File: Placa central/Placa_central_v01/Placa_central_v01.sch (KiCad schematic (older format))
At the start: 79 parts, among them J1 PinoCheckBateriaVcc, J10 Conn_01x01_Arduino11, J11 Conn_01x01_Arduino12, J12 Conn_01x01_Arduino13, J13 Conn_01x01_Arduino14, J14 Conn_01x01_Arduino15, J15 Conn_01x01_Arduino16, J16 PinoChargeBateriaVcc, J17 PinoChargeBateriaGND, J18 Conn_01x01_Arduino19, J19 Conn_01x01_Arduino20, J2 Conn_01x02_ArduinoTxRx, J20 Conn_01x01_Arduino21, J21 Conn_01x01_Arduino22, J22 Conn_01x01_Arduino23, J23 Conn_01x01_Arduino24, J24 Conn_01x01_Arduino25, J25 Conn_01x01_Arduino26, J26 Conn_01x01_Sensor1, J27 Conn_01x01_Sensor2, J28 Conn_01x01_Sensor3, J29 Conn_01x01_Sensor4, J3 Conn_01x01_ArduinoReset, J30 Conn_01x01_Sensor5, J31 Conn_01x01_Sensor6, J32 Conn_01x01_Sensor7, J33 Conn_01x01_SensorEsq, J34 Conn_01x01_SensorDir, J35 Conn_01x01_5VPlacaSensores, J36 Conn_01x01_GNDPlacaSensores, J37 Conn_01x01_8.4VPonteH, J38 Conn_01x01_5VPonteH, J39 Conn_01x01_GNDPonteH, J4 Conn_01x01_Arduino5, J40 Conn_01x01_Motor1PWM, J41 Conn_01x01_Motor1Dir1, J42 Conn_01x01_Motor1Dir2, J43 Conn_01x01_Motor2Dir1, J44 Conn_01x01_Motor2Dir2, J45 Conn_01x01_Motor2PWM, J46 Conn_01x02_Motor1, J47 Conn_01x02_Motor2, J48 Conn_01x01_5VEncoderEsq, J49 Conn_01x01_OutputEncoderEsq, J5 Conn_01x01_Arduino6, J50 Conn_01x01_GNDEncoderEsq, J51 Conn_01x01_5VEncoderDir, J52 Conn_01x01_OutputEncoderDir, J53 Conn_01x01_GNDEncoderDir, J6 Conn_01x01_Arduino7, J7 Conn_01x01_Arduino8, J8 Conn_01x01_Arduino9, J9 Conn_01x01_Arduino10, Q1 BC548, Q2 BC548, SW1 SW_ON/OFF, SW2 SW_AlimentacaoPlacaSensores, SW3 SW_comando1

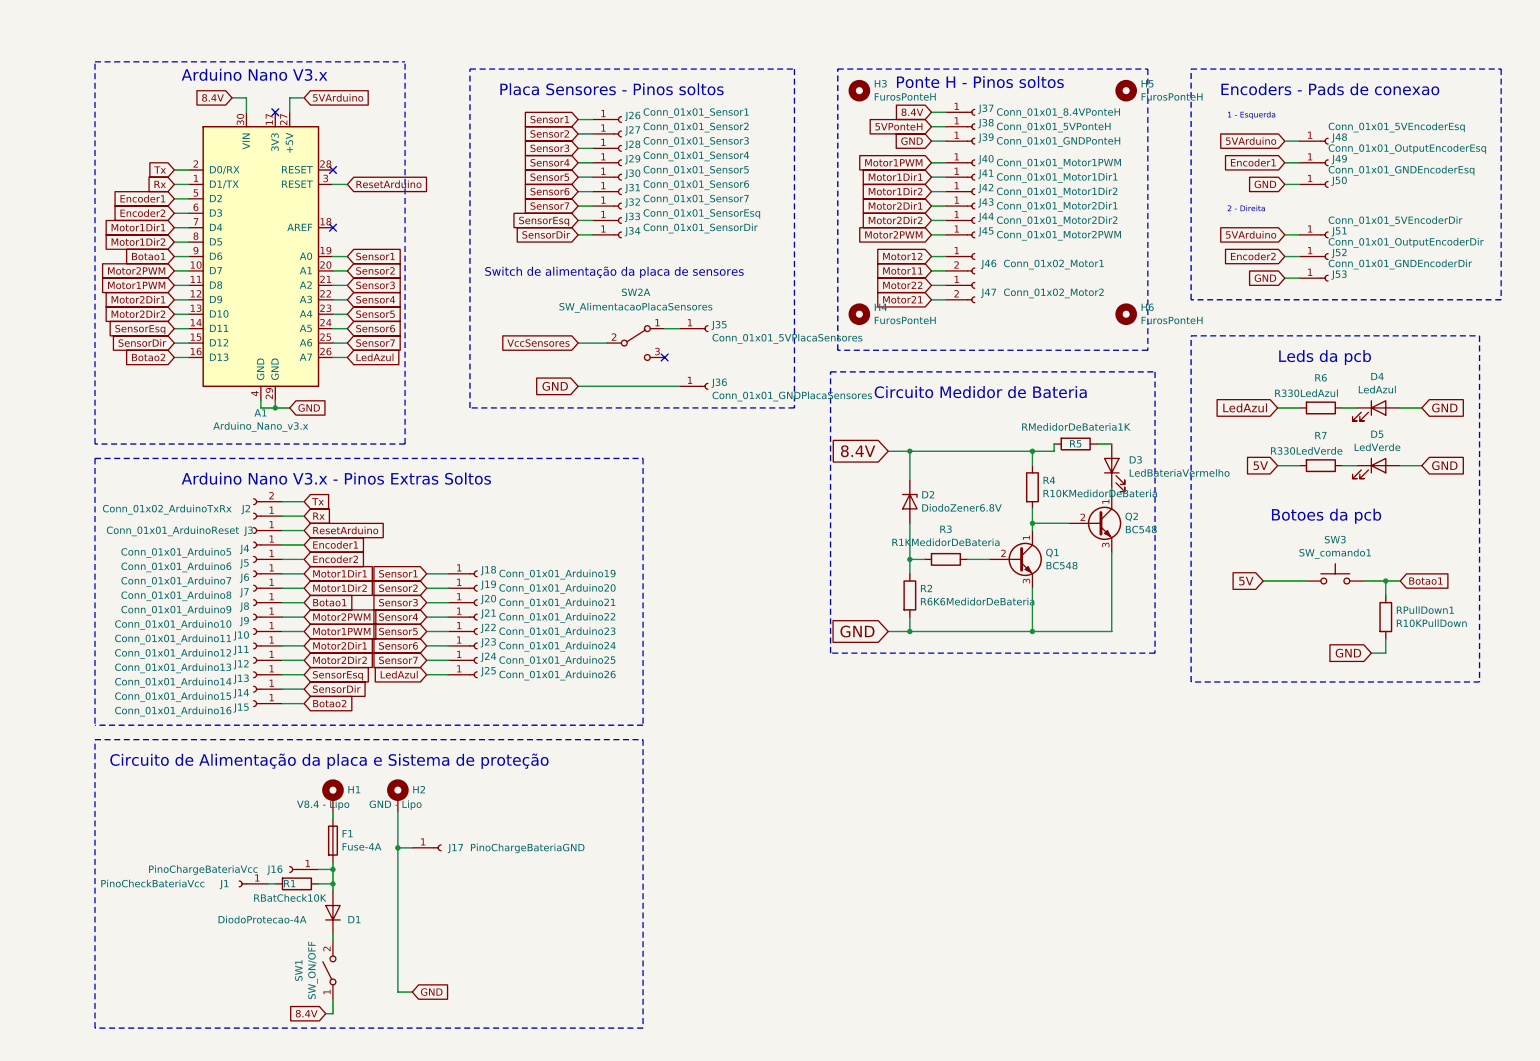
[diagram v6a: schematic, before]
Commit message: Escolha de novos componentes
Acertado quase tudo para o root
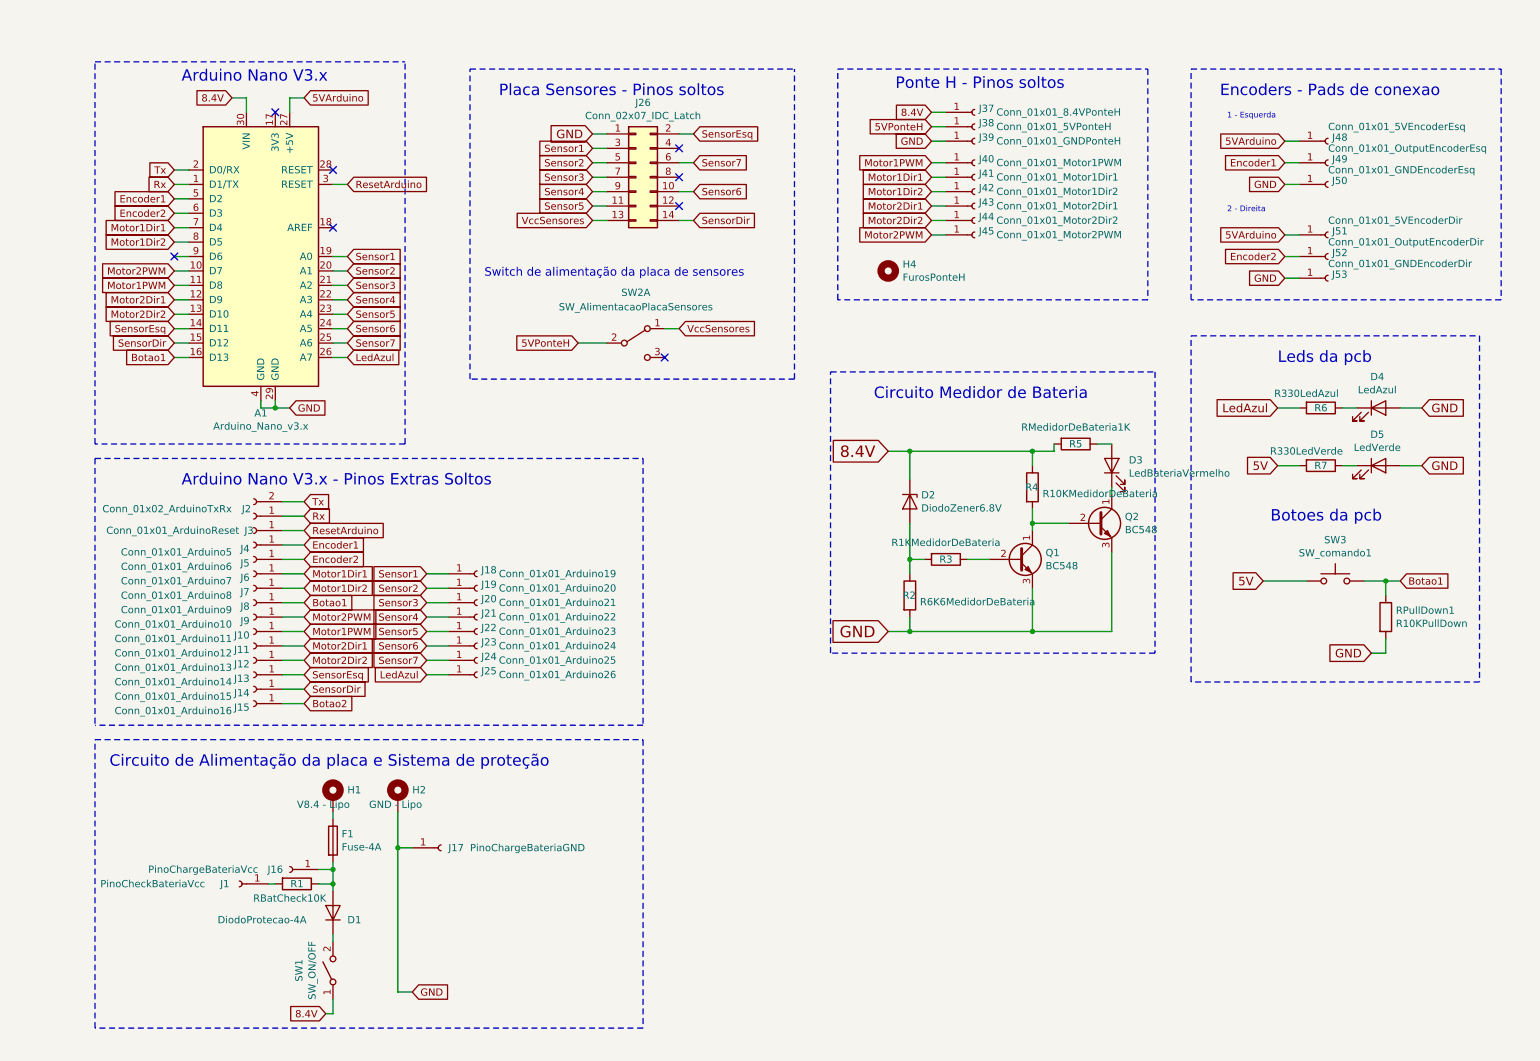
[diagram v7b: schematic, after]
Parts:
- removed H3, H5, H6: FurosPonteH, symbol Mechanical:MountingHole
- removed J26: Conn_01x01_Sensor1, symbol Connector:Conn_01x01_Female
- removed J27: Conn_01x01_Sensor2, symbol Connector:Conn_01x01_Female
- removed J28: Conn_01x01_Sensor3, symbol Connector:Conn_01x01_Female
- removed J29: Conn_01x01_Sensor4, symbol Connector:Conn_01x01_Female
- removed J30: Conn_01x01_Sensor5, symbol Connector:Conn_01x01_Female
- removed J31: Conn_01x01_Sensor6, symbol Connector:Conn_01x01_Female
- removed J32: Conn_01x01_Sensor7, symbol Connector:Conn_01x01_Female
- removed J33: Conn_01x01_SensorEsq, symbol Connector:Conn_01x01_Female
- removed J34: Conn_01x01_SensorDir, symbol Connector:Conn_01x01_Female
- removed J35: Conn_01x01_5VPlacaSensores, symbol Connector:Conn_01x01_Female
- removed J36: Conn_01x01_GNDPlacaSensores, symbol Connector:Conn_01x01_Female
- removed J46: Conn_01x02_Motor1, symbol Connector:Conn_01x02_Female
- removed J47: Conn_01x02_Motor2, symbol Connector:Conn_01x02_Female
- added J26: Conn_02x07_IDC_Latch, Connector_IDC:IDC-Header_2x07_P2.54mm_Horizontal, symbol Connector_Generic:Conn_02x07_Odd_Even
- A1: footprint Module:Arduino_Nano -> Sensores_e_componentes_SL:Arduino_Nano
- D1: footprint (none) -> Diode_THT:D_DO-27_P15.24mm_Horizontal
- D2: footprint (none) -> Diode_THT:D_DO-35_SOD27_P10.16mm_Horizontal
- D3: footprint (none) -> LED_THT:LED_D3.0mm
- D4, D5: footprint Capacitors_THT:CP_Axial_L11.0mm_D5.0mm_P18.00mm_Horizontal -> LED_THT:LED_D3.0mm
- F1: footprint (none) -> Fuse:Fuseholder_Cylinder-5x20mm_Schurter_0031_8201_Horizontal_Open
- H1, H2: footprint (none) -> Connector_Wire:SolderWirePad_1x01_Drill1.5mm
- H4: footprint (none) -> Sensores_e_componentes_SL:Ponte_H_furos
- J1, J10, J11, J12, J13, J14, J15, J18, J19, J20, J21, J22, J23, J24, J25, J3, J4, J49, J5, J52, J6, J7, J8, J9: footprint (none) -> Connector_PinSocket_2.54mm:PinSocket_1x01_P2.54mm_Vertical
- J16, J17: footprint (none) -> Sensores_e_componentes_SL:Jack_Banana
- J2: footprint (none) -> Connector_PinSocket_2.54mm:PinSocket_1x02_P2.54mm_Vertical
- J37, J38, J39: footprint (none) -> Connector_Wire:SolderWirePad_1x01_Drill1.2mm
- J40, J41, J42, J43, J44, J45, J48, J50, J51, J53: footprint (none) -> Connector_Wire:SolderWirePad_1x01_Drill0.8mm
- Q1, Q2: footprint Package_TO_SOT_THT:TO-92_Inline -> Package_TO_SOT_THT:TO-92_Inline_Wide
- R1, R2, R3, R4, R5, R6, R7, RPullDown1: footprint (none) -> Resistor_THT:R_Axial_DIN0207_L6.3mm_D2.5mm_P10.16mm_Horizontal
- SW1: footprint (none) -> Sensores_e_componentes_SL:BotaoOnOff
- SW2: footprint (none) -> Sensores_e_componentes_SL:SW_7x7_6Pinos
- SW3: footprint (none) -> Button_Switch_THT:SW_PUSH_6mm_H5mm
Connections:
- net 5VPonteH: now also SW2.2 (B)
- net Botao1: now also A1.16 (D13); no longer A1.9 (D6)
- net Botao2: no longer A1.16 (D13)
- net GND: now also J26.1 (Pin_1)
- net Sensor1: now also J26.3 (Pin_3)
- net Sensor2: now also J26.5 (Pin_5)
- net Sensor3: now also J26.7 (Pin_7)
- net Sensor4: now also J26.9 (Pin_9)
- net Sensor5: now also J26.11 (Pin_11)
- net Sensor6: now also J26.10 (Pin_10)
- net Sensor7: now also J26.6 (Pin_6)
- net SensorDir: now also J26.14 (Pin_14)
- net SensorEsq: now also J26.2 (Pin_2)
- net VccSensores: now also SW2.1 (A), J26.13 (Pin_13); no longer SW2.2 (B)
- no-connect marks 4 -> 8
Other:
- moved on the sheet: H4

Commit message: Acertado circuito e adicionado fusíveis
Removido o circuito de carga da bateria; retirado os jack; adicionado os fusíveis; e antes de cada motor
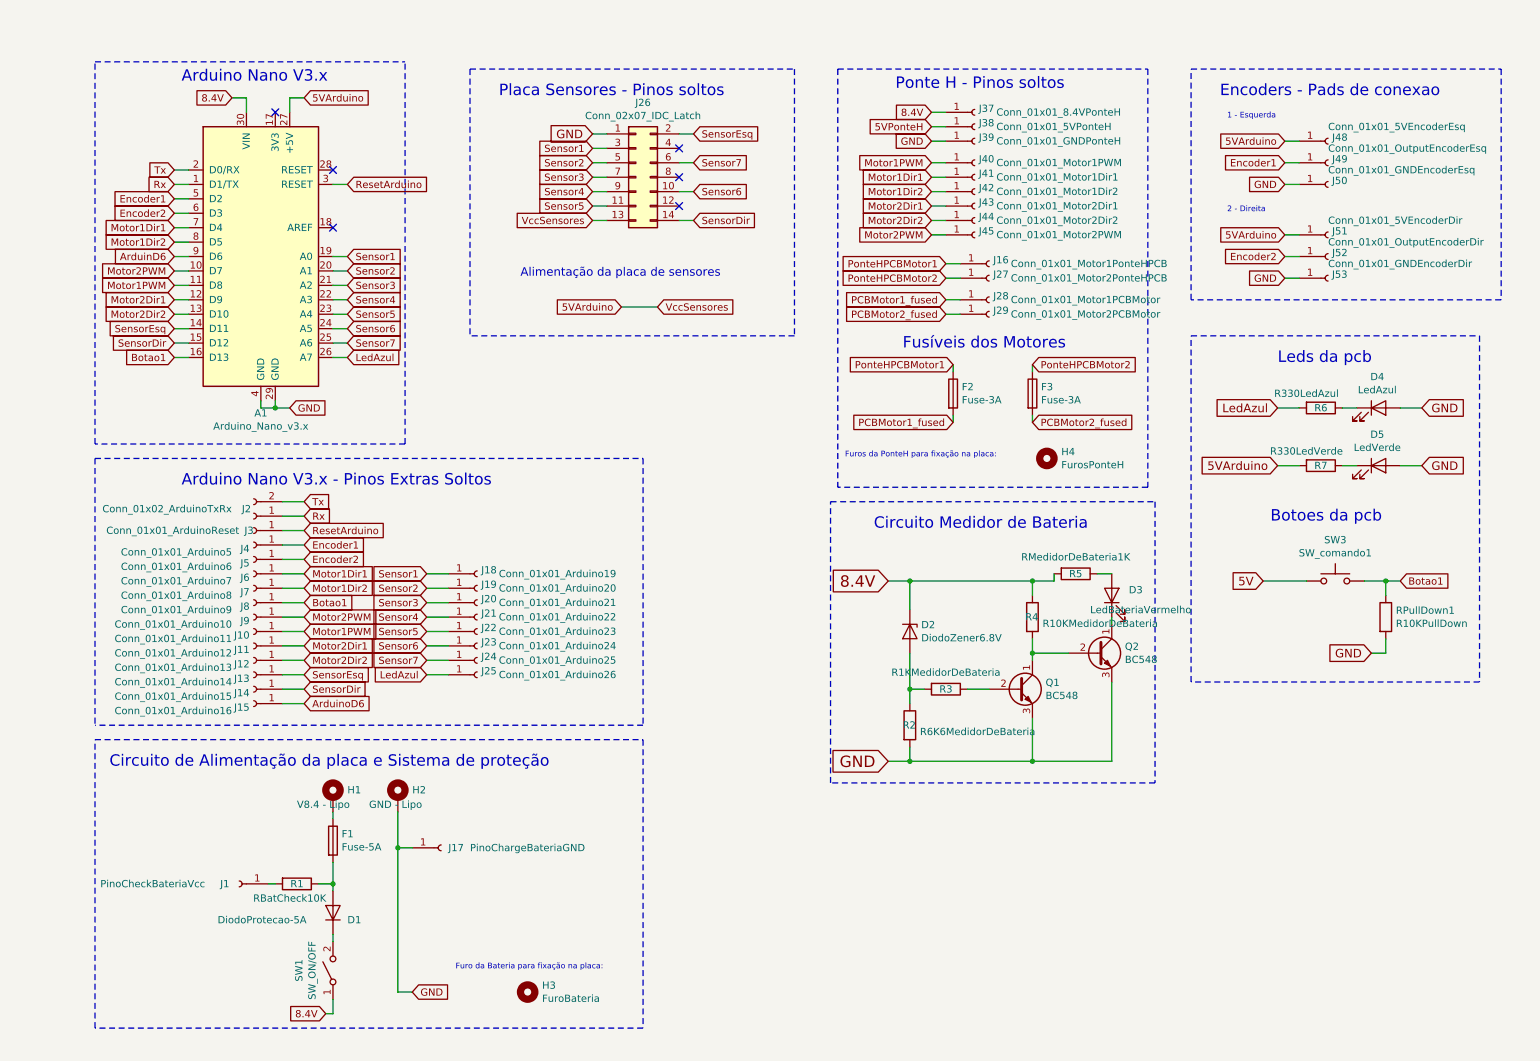
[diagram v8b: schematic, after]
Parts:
- removed SW2: SW_AlimentacaoPlacaSensores, Sensores_e_componentes_SL:SW_7x7_6Pinos, symbol Switch:SW_DPDT_x2
- added F2, F3: Fuse-3A, Fuse:Fuseholder_Cylinder-5x20mm_Stelvio-Kontek_PTF78_Horizontal_Open, symbol Device:Fuse
- added H3: FuroBateria, Sensores_e_componentes_SL:Bateria, symbol Mechanical:MountingHole
- added J27: Conn_01x01_Motor2PonteHPCB, Connector_Wire:SolderWirePad_1x01_Drill1.5mm, symbol Connector:Conn_01x01_Female
- added J28: Conn_01x01_Motor1PCBMotor, Connector_Wire:SolderWirePad_1x01_Drill1.5mm, symbol Connector:Conn_01x01_Female
- added J29: Conn_01x01_Motor2PCBMotor, Connector_Wire:SolderWirePad_1x01_Drill1.5mm, symbol Connector:Conn_01x01_Female
- D1: value DiodoProtecao-4A -> DiodoProtecao-5A
- F1: value Fuse-4A -> Fuse-5A; footprint Fuse:Fuseholder_Cylinder-5x20mm_Schurter_0031_8201_Horizontal_Open -> Fuse:Fuseholder_Cylinder-5x20mm_Stelvio-Kontek_PTF78_Horizontal_Open
- J16: value PinoChargeBateriaVcc -> Conn_01x01_Motor1PonteHPCB; footprint Sensores_e_componentes_SL:Jack_Banana -> Connector_Wire:SolderWirePad_1x01_Drill1.5mm
- J17: footprint Sensores_e_componentes_SL:Jack_Banana -> Connector_Wire:SolderWirePad_1x01_Drill1.5mm
- Q1, Q2: footprint Package_TO_SOT_THT:TO-92_Inline_Wide -> Package_TO_SOT_THT:TO-92_Wide
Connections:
- net VccSensores is gone; now on net 5VArduino: J26.13 (Pin_13)
- net 5V: no longer R7.2
- net 5VArduino: now also R7.2
- net ArduinD6: now reaches A1.9 (D6)
- net at D1.2 (A), F1.2, R1.1: no longer J16.1 (Pin_1)
- net Botao2 renamed ArduinoD6
- new net PCBMotor1_fused: F2.2, J28.1 (Pin_1)
- new net PCBMotor2_fused: F3.2, J29.1 (Pin_1)
- new net PonteHPCBMotor1: F2.1, J16.1 (Pin_1)
- new net PonteHPCBMotor2: F3.1, J27.1 (Pin_1)
- no-connect marks 8 -> 6
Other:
- note added: "Alimentação da placa de sensores"
- note added: "Furo da Bateria para fixação na placa:"
- note added: "Furos da PonteH para fixação na placa:"
- note added: "Fusíveis dos Motores"
- note removed: "Switch de alimentação da placa de sensores"
- moved on the sheet: D2, D3, H4, Q1, Q2, R2, R3, R4, R5
